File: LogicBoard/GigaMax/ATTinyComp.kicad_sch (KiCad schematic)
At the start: 11 parts, among them J21 UARTDBG, U16 ATTINY1616-MNR, U2 TPL0401B-10DCKR

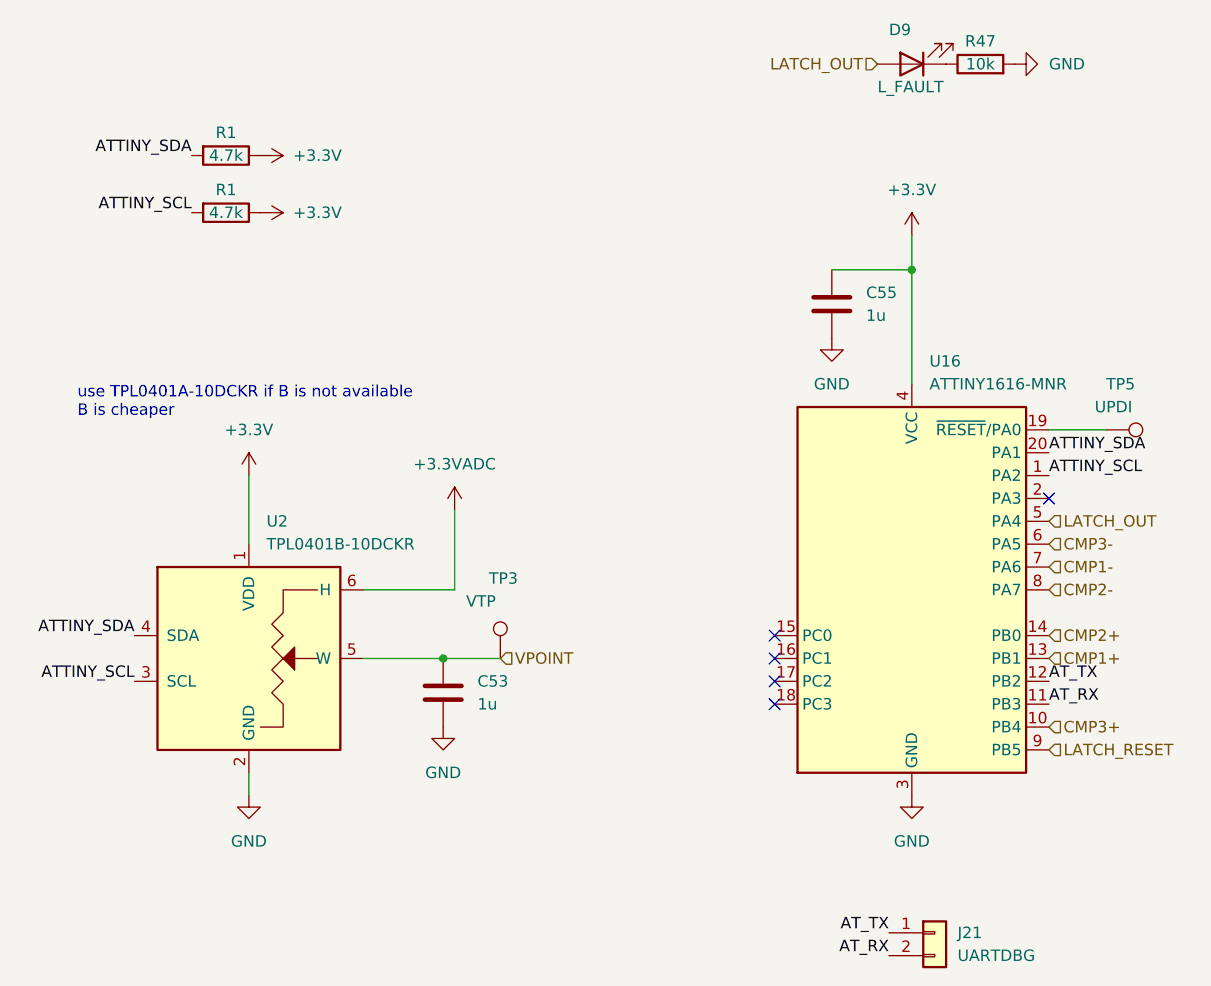
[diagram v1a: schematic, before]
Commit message: v2.8.0 - Small Hall sensors
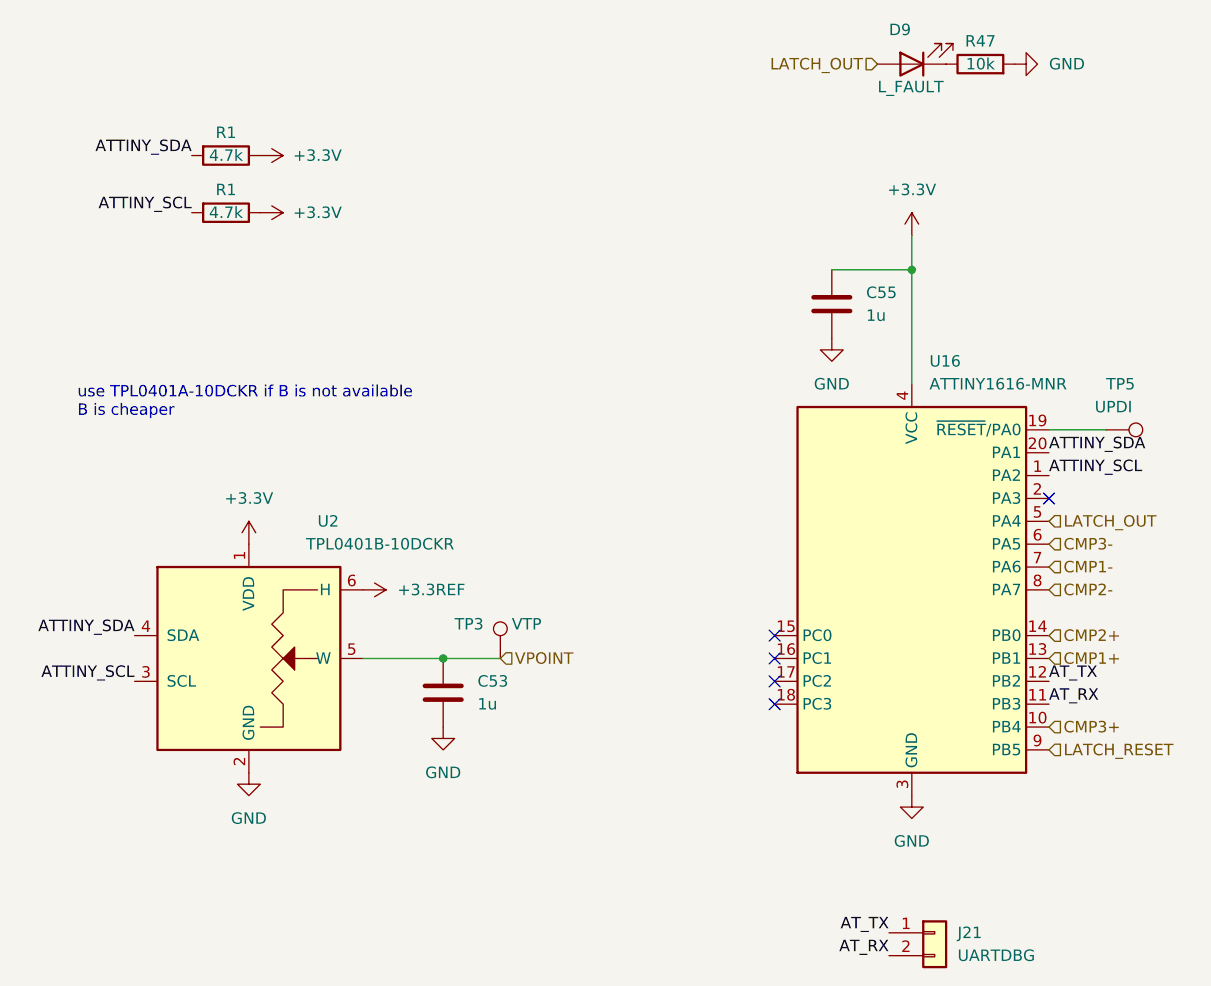
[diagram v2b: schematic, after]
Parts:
- C53, C55: footprint Capacitor_SMD:C_0402_1005Metric -> GigaVescLibs:C_0603_1608Metric_L; MPN C52923 -> C15849
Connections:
- net +3.3VADC renamed +3.3REF
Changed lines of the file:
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@@
   (no_connect (at 129.54 96.52))
   (no_connect (at 129.54 99.06))
-  (wire (pts (xy 71.12 76.2) (xy 71.12 83.82))
-    (stroke (width 0) (type default))
-  )
   (wire (pts (xy 144.78 53.34) (xy 144.78 66.04))
     (stroke (width 0) (type default))
   )
-  (wire (pts (xy 71.12 109.22) (xy 71.12 111.76))
-    (stroke (width 0) (type default))
-  )
   (wire (pts (xy 135.89 53.34) (xy 144.78 53.34))
     (stroke (width 0) (type default))
   )
-  (wire (pts (xy 93.98 80.01) (xy 93.98 88.9))
-    (stroke (width 0) (type default))
-  )
   (wire (pts (xy 160.02 71.12) (xy 166.37 71.12))
     (stroke (width 0) (type default))
@@
   )
   (wire (pts (xy 92.71 96.52) (xy 99.06 96.52))
-    (stroke (width 0) (type default))
-  )
-  (wire (pts (xy 93.98 88.9) (xy 83.82 88.9))
     (stroke (width 0) (type default))
   )
@@
     )
   )
-  (symbol (lib_id "power:+3.3V") (at 71.12 76.2 0) (unit 1)
-    (in_bom yes) (on_board yes) (dnp no) (fields_autoplaced)
-    (property "Reference" "#PWR085" (at 71.12 80.01 0)
-      (effects (font (size 1.27 1.27)) hide)
-    )
-    (property "Value" "+3.3V" (at 71.12 71.12 0)
-      (effects (font (size 1.27 1.27)))
-    )
-    (property "Footprint" "" (at 71.12 76.2 0)
-      (effects (font (size 1.27 1.27)) hide)
-    )
-    (property "Datasheet" "" (at 71.12 76.2 0)
+  (symbol (lib_id "power:+3.3V") (at 71.12 83.82 0) (unit 1)
+    (in_bom yes) (on_board yes) (dnp no) (fields_autoplaced)
+    (property "Reference" "#PWR085" (at 71.12 87.63 0)
+      (effects (font (size 1.27 1.27)) hide)
+    )
+    (property "Value" "+3.3V" (at 71.12 78.74 0)
+      (effects (font (size 1.27 1.27)))
+    )
+    (property "Footprint" "" (at 71.12 83.82 0)
+      (effects (font (size 1.27 1.27)) hide)
+    )
+    (property "Datasheet" "" (at 71.12 83.82 0)
       (effects (font (size 1.27 1.27)) hide)
     )
@@
     )
   )
-  (symbol (lib_id "power:+3.3VADC") (at 93.98 80.01 0) (unit 1)
-    (in_bom yes) (on_board yes) (dnp no) (fields_autoplaced)
-    (property "Reference" "#PWR0127" (at 97.79 81.28 0)
-      (effects (font (size 1.27 1.27)) hide)
-    )
-    (property "Value" "+3.3VADC" (at 93.98 74.93 0)
-      (effects (font (size 1.27 1.27)))
-    )
-    (property "Footprint" "" (at 93.98 80.01 0)
-      (effects (font (size 1.27 1.27)) hide)
-    )
-    (property "Datasheet" "" (at 93.98 80.01 0)
-      (effects (font (size 1.27 1.27)) hide)
-    )
-    (pin "1")
-    (instances
-      (project "GigaMax"
-        (path "/768a484b-8a27-40cf-8cad-0f63935b1af0/81081265-f675-4f9d-bffe-8ec1eaaaba23"
-          (reference "#PWR0127") (unit 1)
-        )
-        (path "/768a484b-8a27-40cf-8cad-0f63935b1af0/81081265-f675-4f9d-bffe-8ec1eaaaba23/4e84f19f-3250-45a9-9b88-20e811e150a6"
-          (reference "#PWR085") (unit 1)
-        )
-        (path "/768a484b-8a27-40cf-8cad-0f63935b1af0/81081265-f675-4f9d-bffe-8ec1eaaaba23/ac734765-aa76-45cd-b5a0-b23ad6c1564a"
-          (reference "#PWR0129") (unit 1)
-        )
-      )
-      (project "HardwareProtection"
-        (path "/a0bc7e80-607b-4b14-b86e-d486e2d36eac"
-          (reference "#PWR014") (unit 1)
-        )
-      )
-    )
-  )
   (symbol (lib_id "Potentiometer_Digital:TPL0401B-10-Q1") (at 71.12 96.52 0) (unit 1)
-    (in_bom yes) (on_board yes) (dnp no) (fields_autoplaced)
-    (property "Reference" "U2" (at 73.0759 81.28 0)
-      (effects (font (size 1.27 1.27)) (justify left))
-    )
-    (property "Value" "TPL0401B-10DCKR" (at 73.0759 83.82 0)
+    (in_bom yes) (on_board yes) (dnp no)
+    (property "Reference" "U2" (at 78.74 81.28 0)
+      (effects (font (size 1.27 1.27)) (justify left))
+    )
+    (property "Value" "TPL0401B-10DCKR" (at 77.47 83.82 0)
       (effects (font (size 1.27 1.27)) (justify left))
     )
@@
   (symbol (lib_id "Connector:TestPoint") (at 99.06 96.52 0) (unit 1)
     (in_bom yes) (on_board yes) (dnp no)
-    (property "Reference" "TP3" (at 97.79 87.63 0)
-      (effects (font (size 1.27 1.27)) (justify left))
-    )
-    (property "Value" "VTP" (at 95.25 90.17 0)
+    (property "Reference" "TP3" (at 93.98 92.71 0)
+      (effects (font (size 1.27 1.27)) (justify left))
+    )
+    (property "Value" "VTP" (at 100.33 92.71 0)
       (effects (font (size 1.27 1.27)) (justify left))
     )
@@
     )
   )
-  (symbol (lib_id "power:GND") (at 71.12 111.76 0) (unit 1)
-    (in_bom yes) (on_board yes) (dnp no) (fields_autoplaced)
-    (property "Reference" "#PWR088" (at 71.12 118.11 0)
-      (effects (font (size 1.27 1.27)) hide)
-    )
-    (property "Value" "GND" (at 71.12 116.84 0)
-      (effects (font (size 1.27 1.27)))
-    )
-    (property "Footprint" "" (at 71.12 111.76 0)
-      (effects (font (size 1.27 1.27)) hide)
-    )
-    (property "Datasheet" "" (at 71.12 111.76 0)
+  (symbol (lib_id "GigaVescSymbols:+3.3REF") (at 83.82 88.9 270) (unit 1)
+    (in_bom yes) (on_board yes) (dnp no) (fields_autoplaced)
+    (property "Reference" "#PWR017" (at 80.01 88.9 0)
+      (effects (font (size 1.27 1.27)) hide)
+    )
+    (property "Value" "+3.3REF" (at 87.63 88.9 90)
+      (effects (font (size 1.27 1.27)) (justify left))
+    )
+    (property "Footprint" "" (at 83.82 88.9 0)
+      (effects (font (size 1.27 1.27)) hide)
+    )
+    (property "Datasheet" "" (at 83.82 88.9 0)
+      (effects (font (size 1.27 1.27)) hide)
+    )
+    (pin "1")
+    (instances
+      (project "GigaMax"
+        (path "/768a484b-8a27-40cf-8cad-0f63935b1af0/717cb4b7-b47a-435c-946f-7c938a1d7e5f"
+          (reference "#PWR017") (unit 1)
+        )
+        (path "/768a484b-8a27-40cf-8cad-0f63935b1af0/81081265-f675-4f9d-bffe-8ec1eaaaba23/ac734765-aa76-45cd-b5a0-b23ad6c1564a"
+          (reference "#PWR017") (unit 1)
+        )
+        (path "/768a484b-8a27-40cf-8cad-0f63935b1af0/81081265-f675-4f9d-bffe-8ec1eaaaba23/4e84f19f-3250-45a9-9b88-20e811e150a6"
+          (reference "#PWR0203") (unit 1)
+        )
+      )
+    )
+  )
+  (symbol (lib_id "power:GND") (at 71.12 109.22 0) (unit 1)
+    (in_bom yes) (on_board yes) (dnp no) (fields_autoplaced)
+    (property "Reference" "#PWR088" (at 71.12 115.57 0)
+      (effects (font (size 1.27 1.27)) hide)
+    )
+    (property "Value" "GND" (at 71.12 114.3 0)
+      (effects (font (size 1.27 1.27)))
+    )
+    (property "Footprint" "" (at 71.12 109.22 0)
+      (effects (font (size 1.27 1.27)) hide)
+    )
+    (property "Datasheet" "" (at 71.12 109.22 0)
       (effects (font (size 1.27 1.27)) hide)
     )
@@
       (effects (font (size 1.27 1.27)) (justify left))
     )
-    (property "Footprint" "Capacitor_SMD:C_0402_1005Metric" (at 93.6752 104.14 0)
+    (property "Footprint" "GigaVescLibs:C_0603_1608Metric_L" (at 93.6752 104.14 0)
       (effects (font (size 1.27 1.27)) hide)
     )
@@
       (effects (font (size 1.27 1.27)) hide)
     )
-    (property "MPN" "C52923" (at 92.71 100.33 0)
+    (property "MPN" "C15849" (at 92.71 100.33 0)
       (effects (font (size 1.27 1.27)) hide)
     )
@@
       (effects (font (size 1.27 1.27)) (justify left))
     )
-    (property "Footprint" "Capacitor_SMD:C_0402_1005Metric" (at 136.8552 60.96 0)
+    (property "Footprint" "GigaVescLibs:C_0603_1608Metric_L" (at 136.8552 60.96 0)
       (effects (font (size 1.27 1.27)) hide)
     )
@@
       (effects (font (size 1.27 1.27)) hide)
     )
-    (property "MPN" "C52923" (at 135.89 57.15 0)
-      (effects (font (size 1.27 1.27)) hide)
-    )
+    (property "MPN" "C15849" (at 135.89 57.15 0)
+      (effects (font (size 1.27 1.27)) hide)
+    )
